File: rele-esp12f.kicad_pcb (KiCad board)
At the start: 2 copper layers, 66 x 66 mm, 31 parts, among them J1 N / L_OUT / L_IN, J3 PROG, K1 SRD-05VDC-SL-C, Q1 SS8050, SW1 TS-1187A, SW2 TS-1187A, U1 AMS1117-3.3, U2 ESP-12F

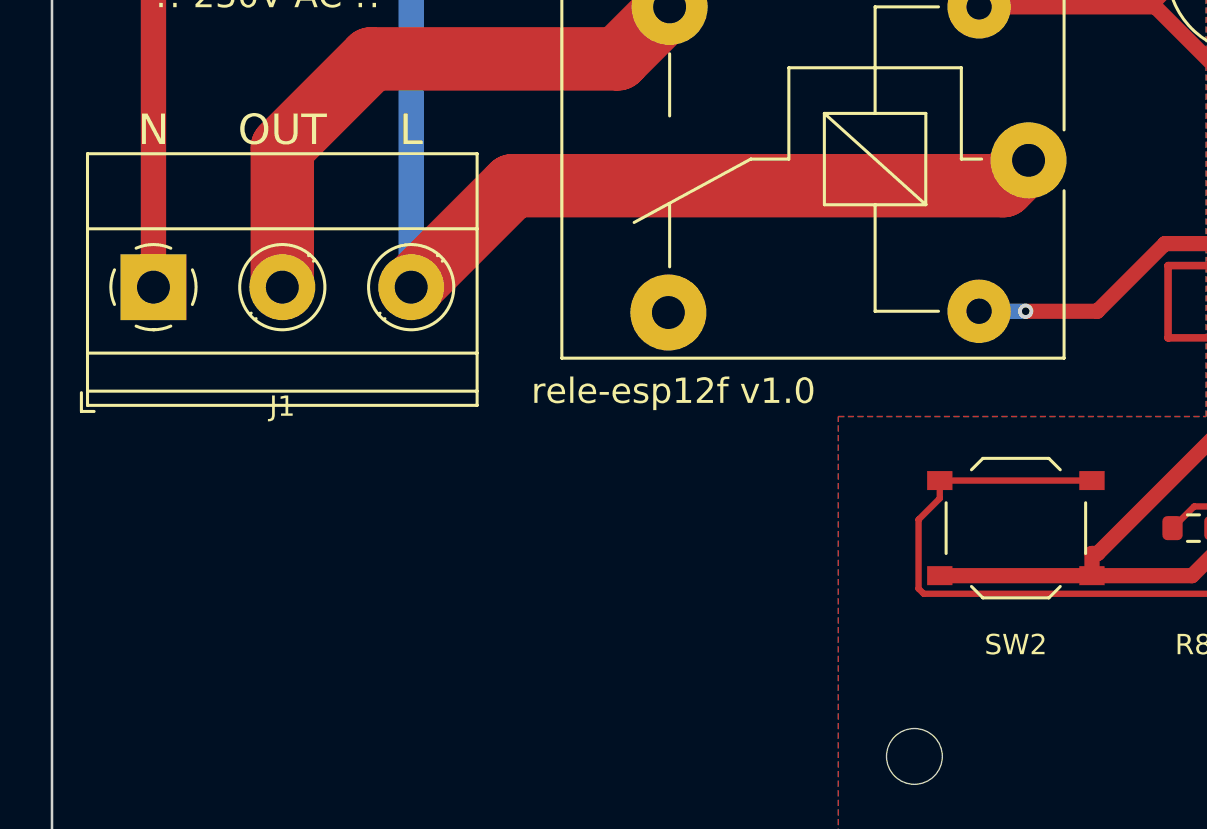
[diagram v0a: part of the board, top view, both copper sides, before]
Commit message: Adjust layout of mains traces L_IN, N and L_OUT
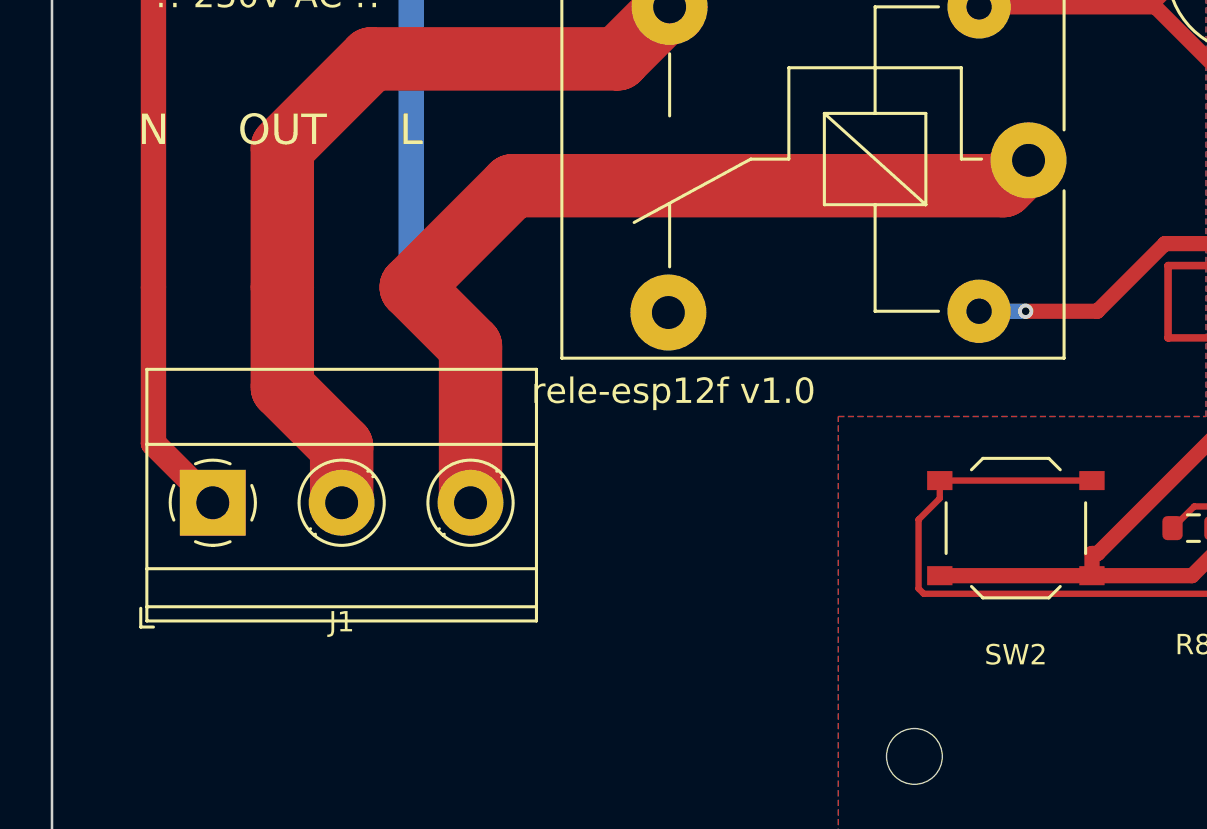
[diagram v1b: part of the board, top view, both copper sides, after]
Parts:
- moved J1 8.82 mm to (106.3, 151.0)
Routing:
- net N: track 59.1 -> 68.5 mm
- net L_OUT: track 23.1 -> 32.5 mm
- net L_IN: track 43.5 -> 53.0 mm
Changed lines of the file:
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@@
 	(footprint "TerminalBlock_Phoenix:TerminalBlock_Phoenix_MKDS-1,5-3-5.08_1x03_P5.08mm_Horizontal"
 		(layer "F.Cu")
-		(at 104 142.5)
+		(at 106.34 151)
 		(descr "Terminal Block Phoenix MKDS-1,5-3-5.08, 3 pins, pitch 5.08mm, size 15.2x9.8mm^2, drill diamater 1.3mm, pad diameter 2.6mm, see http://www.farnell.com/datasheets/100425.pdf, script-generated using https://github.com/pointhi/kicad-footprint-generator/scripts/TerminalBlock_Phoenix")
 		(tags "THT Terminal Block Phoenix MKDS-1,5-3-5.08 pitch 5.08mm size 15.2x9.8mm^2 drill 1.3mm pad 2.6mm")
@@
 		)
 		(property "Value" "LED relay (rojo)"
-			(at 0 1.43 0)
+			(at 0.5 2.5 0)
 			(layer "F.Fab")
 			(effects
@@
 		(tags "SPST Tactile Switch")
 		(property "Reference" "SW2"
-			(at 0 4.6 0)
+			(at 0 5 0)
 			(layer "F.SilkS")
 			(effects
@@
 	)
 	(segment
+		(start 114.16 142.5)
+		(end 116.5 144.84)
+		(width 2.5)
+		(layer "F.Cu")
+		(net "L_IN")
+	)
+	(segment
+		(start 116.5 144.84)
+		(end 116.5 151)
+		(width 2.5)
+		(layer "F.Cu")
+		(net "L_IN")
+	)
+	(segment
 		(start 112 126.3)
 		(end 114.16 128.46)
@@
 	)
 	(segment
+		(start 104 148.66)
+		(end 106.34 151)
+		(width 1)
+		(layer "F.Cu")
+		(net "N")
+	)
+	(segment
+		(start 104 142.5)
+		(end 104 148.66)
+		(width 1)
+		(layer "F.Cu")
+		(net "N")
+	)
+	(segment
 		(start 104 142.5)
 		(end 104 116)
@@
 		(layer "F.Cu")
 		(net "L_OUT")
+	)
+	(segment
+		(start 111.42 148.79)
+		(end 111.42 151)
+		(width 2.5)
+		(layer "F.Cu")
+		(net "L_OUT")
+	)
+	(segment
+		(start 109.08 142.5)
+		(end 109.08 146.45)
+		(width 2.5)
+		(layer "F.Cu")
+		(net "L_OUT")
+	)
+	(segment
+		(start 109.08 146.45)
+		(end 111.42 148.79)
+		(width 2.5)
+		(layer "F.Cu")
+		(net "L_OUT")

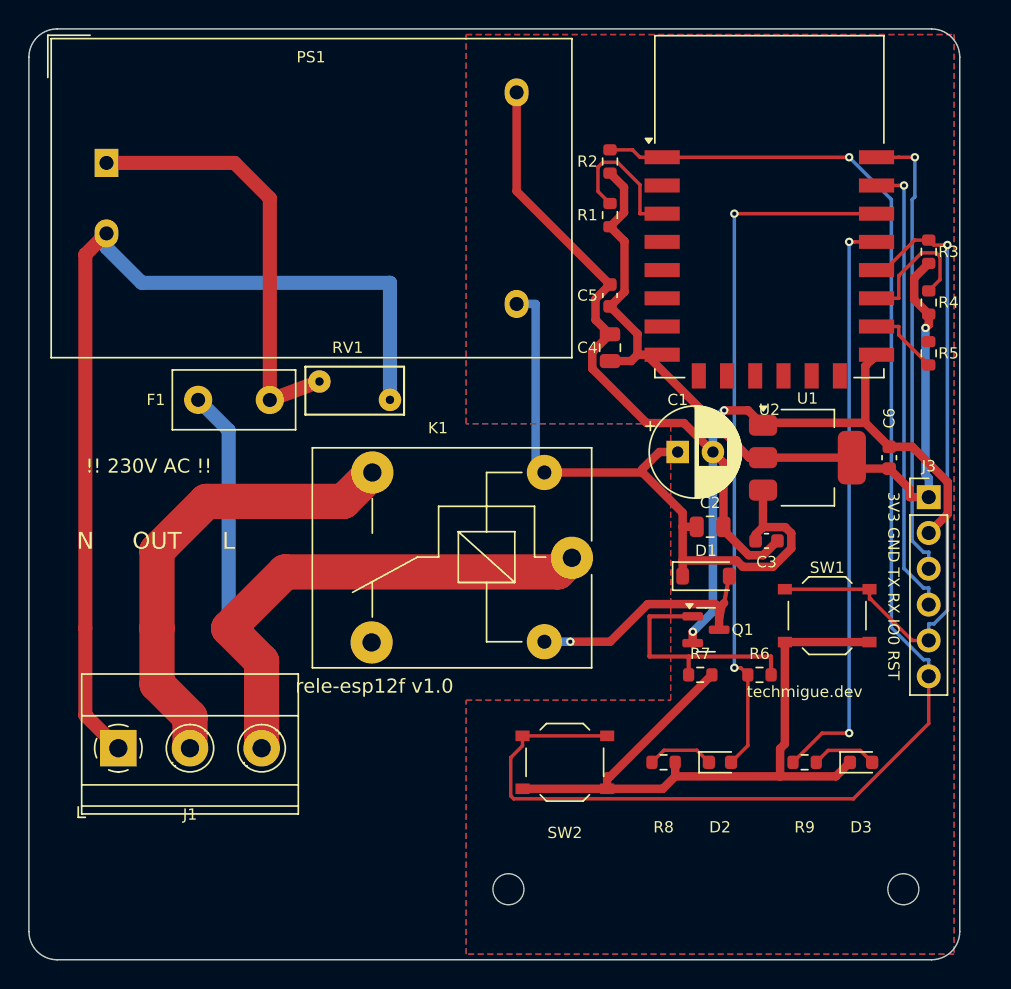
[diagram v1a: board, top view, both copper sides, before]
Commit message: v2 redesign: 66.5 x 44 mm board and 110 VAC
  New layout (PS1 and ESP-12F at the top, mains zone at the bottom left
  and low voltage at the bottom right), J3 as a 2x3 header, board nets
  synchronized with the schematic and MAINS/PWR net classes extended to
  the new names, GND planes on both sides restricted to the low-voltage
  zone. BOM, CPL, gerbers, renders and README updated.
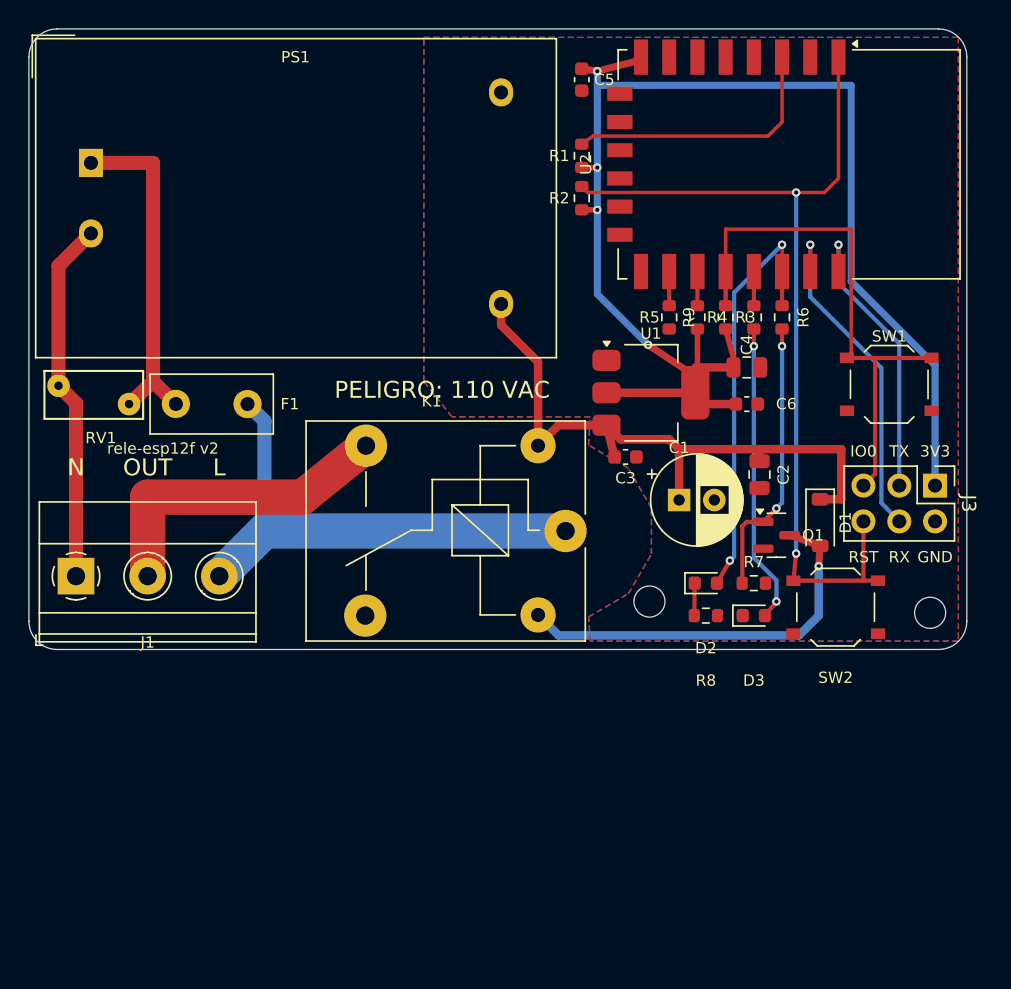
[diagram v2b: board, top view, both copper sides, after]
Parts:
- J3: footprint Connector_PinHeader_2.54mm:PinHeader_1x06_P2.54mm_Vertical -> Connector_PinHeader_2.54mm:PinHeader_2x03_P2.54mm_Vertical
- R9: value 1k -> 220
- RV1: value 07D471K -> 07D221K
- moved R9 31.8 mm to (151.4, 120.5), turned to -90 degrees
- moved R6 25.4 mm to (153.4, 120.5), turned to -90 degrees
- moved MH1 22.7 mm to (144.0, 140.6)
- moved SW2 22.1 mm to (157.2, 141.0)
- moved MH2 19.7 mm to (163.9, 141.4)
- moved R5 18.6 mm to (145.4, 120.5), turned to -90 degrees
- moved SW1 17.0 mm to (161.0, 125.2)
- moved R4 16.4 mm to (147.4, 120.5)
- moved C5 15.4 mm to (139.2, 103.6), turned to -90 degrees
- moved R3 15.1 mm to (149.4, 120.5)
- moved RV1 13.6 mm to (107.1, 126.6), turned to 180 degrees
- moved D3 12.9 mm to (151.4, 141.6)
- moved D2 12.7 mm to (148.0, 139.3)
- moved J1 12.6 mm to (103.3, 138.8)
- moved U1 12.0 mm to (144.1, 125.8)
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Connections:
- net COIL_N renamed /COIL_N
- net EN renamed /EN
- net GPIO0 renamed /GPIO0
- net GPIO15 renamed /GPIO15
- net GPIO2 renamed /GPIO2
- net LED_RELAY_K renamed Net-(D2-K)
- net LED_WIFI_A renamed Net-(D3-A)
- net L_F renamed /L_F
- net L_IN renamed /L_IN
- net L_OUT renamed /L_OUT
- net N renamed /N
- net Q1_B renamed Net-(Q1-B)
- net RELAY renamed /RELAY
- net RST renamed /RST
- net RXD renamed /RXD
- net TXD renamed /TXD
- net WIFI_LED renamed /WIFI_LED
- K1 pad 4: (no net) -> unconnected-(K1-Pad4)
- U2 pad 10: (no net) -> unconnected-(U2-MISO-Pad10)
- U2 pad 11: (no net) -> unconnected-(U2-GPIO9-Pad11)
- U2 pad 12: (no net) -> unconnected-(U2-GPIO10-Pad12)
- U2 pad 13: (no net) -> unconnected-(U2-MOSI-Pad13)
- U2 pad 14: (no net) -> unconnected-(U2-SCLK-Pad14)
- U2 pad 2: (no net) -> unconnected-(U2-ADC-Pad2)
- U2 pad 4: (no net) -> unconnected-(U2-GPIO16-Pad4)
- U2 pad 5: (no net) -> unconnected-(U2-GPIO14-Pad5)
- U2 pad 6: (no net) -> unconnected-(U2-GPIO12-Pad6)
- U2 pad 7: (no net) -> unconnected-(U2-GPIO13-Pad7)
- U2 pad 9: (no net) -> unconnected-(U2-CS0-Pad9)
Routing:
- net GND: track 142.3 -> 0.00 mm, vias 2 -> 0
- net /N: track 68.5 -> 25.8 mm
- net /WIFI_LED: track 41.6 -> 2.42 mm, vias 2 -> 0
- net /RST: track 102.4 -> 64.1 mm, vias 1 -> 2
- net +3V3: track 61.4 -> 96.1 mm, vias 1 -> 4
- net /RELAY: track 50.1 -> 28.9 mm
- net /L_IN: track 53.0 -> 35.4 mm
- net Net-(D3-A): track 4.66 -> 21.3 mm, vias 0 -> 2
- net /TXD: track 32.7 -> 19.6 mm
- net /L_OUT: track 32.5 -> 22.4 mm
- net /RXD: track 32.6 -> 22.9 mm
- net /GPIO0: track 47.0 -> 37.8 mm, vias 1 -> 0
- net /COIL_N: track 19.5 -> 28.3 mm
- net /EN: track 10.3 -> 18.4 mm
- net /GPIO2: track 9.64 -> 2.42 mm
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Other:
- board size 66 x 66 mm -> 66.5 x 44 mm
- board text added: "3V3"
- board text added: "GND"
- board text added: "IO0"
- board text added: "PELIGRO: 110 VAC"
- board text added: "RST"
- board text added: "RX"
- board text added: "TX"
- board text added: "rele-esp12f v2"
- board text removed: "!! 230V AC !!"
- board text removed: "3V3 GND TX RX IO0 RST"
- board text removed: "rele-esp12f v1.0"
- board text removed: "techmigue.dev"
